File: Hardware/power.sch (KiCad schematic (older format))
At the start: 9 parts, among them J1 Barrel_Jack, U4 TL074, U5 LD1117S33CTR

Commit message: complete initial PCB layout. CapSense buttons still not done, but everything else should be there. I had to increase to a 4-layer board to keep the dimensions 8"x4".
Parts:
- removed D1: D, digikey-footprints:TO-252-3, symbol D
- added D1: D_Schottky, Diodes_SMD:D_SMB, symbol D_Schottky
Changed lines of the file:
@@
 Wire Wire Line
 	2150 1800 2100 1800
-$Comp
-L D D1
-U 1 1 5C392341
-P 2450 1600
-F 0 "D1" H 2450 1700 50  0000 C CNN
-F 1 "D" H 2450 1500 50  0000 C CNN
-F 2 "digikey-footprints:TO-252-3" H 2450 1600 50  0001 C CNN
-F 3 "" H 2450 1600 50  0001 C CNN
-	1    2450 1600
-	-1   0    0    1
-$EndComp
 Wire Wire Line
 	2700 1500 2700 1600
@@
 	1    0    0    1
 $EndComp
+$Comp
+L D_Schottky D1
+U 1 1 5C40562C
+P 2450 1600
+F 0 "D1" H 2450 1700 50  0000 C CNN
+F 1 "D_Schottky" H 2450 1500 50  0000 C CNN
+F 2 "Diodes_SMD:D_SMB" H 2450 1600 50  0001 C CNN
+F 3 "" H 2450 1600 50  0001 C CNN
+	1    2450 1600
+	-1   0    0    1
+$EndComp
 $EndSCHEMATC

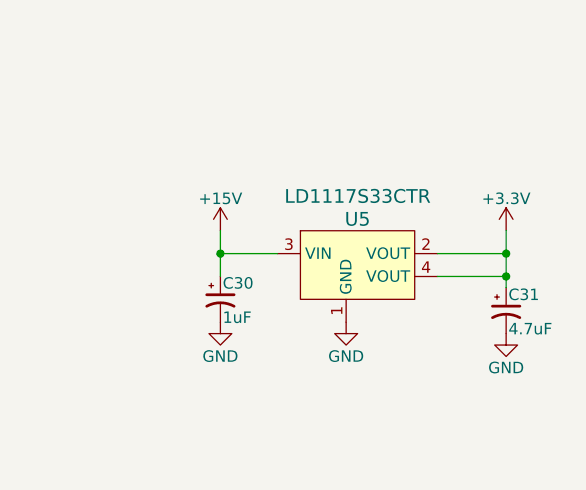
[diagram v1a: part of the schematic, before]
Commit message: change 3.3V to 5V, fix LFO biasing, LPF, JFET bias trim pots.
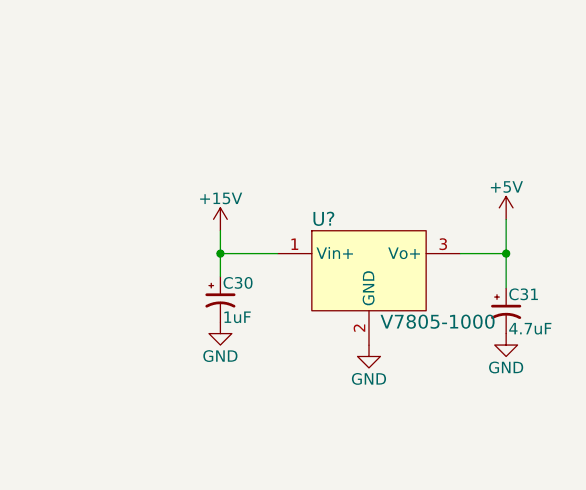
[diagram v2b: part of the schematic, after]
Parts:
- removed U5: LD1117S33CTR, digikey-footprints:SOT-223, symbol LD1117S33CTR
- added U?: V7805-1000, digikey-footprints:3-SIP_Module_V7805-1000, symbol V7805-1000
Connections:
- net +15V: now also U?.1 (Vin+)
- net GND: now also U?.2 (GND)
- net +3V3 renamed +5V
- net +5V: now also U?.3 (Vo+)
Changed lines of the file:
@@
 Connection ~ 1900 3150
-$Comp
-L LD1117S33CTR U5
-U 1 1 5C392D20
-P 5250 2750
-F 0 "U5" H 5300 2900 60  0000 C CNN
-F 1 "LD1117S33CTR" H 5300 3000 60  0000 C CNN
-F 2 "digikey-footprints:SOT-223" H 5450 2950 60  0001 L CNN
-F 3 "http://www.st.com/content/ccc/resource/technical/document/datasheet/99/3b/7d/91/91/51/4b/be/CD00000544.pdf/files/CD00000544.pdf/jcr:content/translations/en.CD00000544.pdf" H 5450 3050 60  0001 L CNN
-F 4 "497-1241-1-ND" H 5450 3150 60  0001 L CNN "Digi-Key_PN"
-F 5 "LD1117S33CTR" H 5450 3250 60  0001 L CNN "MPN"
-F 6 "Integrated Circuits (ICs)" H 5450 3350 60  0001 L CNN "Category"
-F 7 "PMIC - Voltage Regulators - Linear" H 5450 3450 60  0001 L CNN "Family"
-F 8 "http://www.st.com/content/ccc/resource/technical/document/datasheet/99/3b/7d/91/91/51/4b/be/CD00000544.pdf/files/CD00000544.pdf/jcr:content/translations/en.CD00000544.pdf" H 5450 3550 60  0001 L CNN "DK_Datasheet_Link"
-F 9 "/product-detail/en/stmicroelectronics/LD1117S33CTR/497-1241-1-ND/586241" H 5450 3650 60  0001 L CNN "DK_Detail_Page"
-F 10 "IC REG LINEAR 3.3V 800MA SOT223" H 5450 3750 60  0001 L CNN "Description"
-F 11 "STMicroelectronics" H 5450 3850 60  0001 L CNN "Manufacturer"
-F 12 "Active" H 5450 3950 60  0001 L CNN "Status"
-	1    5250 2750
-	1    0    0    -1
-$EndComp
 $Comp
 L CP1_Small C30
@@
 L GND #PWR044
 U 1 1 5C392F13
-P 5250 3050
-F 0 "#PWR044" H 5250 2800 50  0001 C CNN
-F 1 "GND" H 5250 2900 50  0000 C CNN
-F 2 "" H 5250 3050 50  0001 C CNN
-F 3 "" H 5250 3050 50  0001 C CNN
-	1    5250 3050
+P 5350 3150
+F 0 "#PWR044" H 5350 2900 50  0001 C CNN
+F 1 "GND" H 5350 3000 50  0000 C CNN
+F 2 "" H 5350 3150 50  0001 C CNN
+F 3 "" H 5350 3150 50  0001 C CNN
+	1    5350 3150
 	1    0    0    -1
 $EndComp
-$Comp
-L +3.3V #PWR045
-U 1 1 5C392F35
-P 5950 2650
-F 0 "#PWR045" H 5950 2500 50  0001 C CNN
-F 1 "+3.3V" H 5950 2790 50  0000 C CNN
-F 2 "" H 5950 2650 50  0001 C CNN
-F 3 "" H 5950 2650 50  0001 C CNN
-	1    5950 2650
-	1    0    0    -1
-$EndComp
-Wire Wire Line
-	5950 2650 5950 2900
-Wire Wire Line
-	5950 2750 5650 2750
-Wire Wire Line
-	5950 2850 5650 2850
-Connection ~ 5950 2750
 $Comp
 L CP1_Small C31
@@
 	1    0    0    -1
 $EndComp
-Connection ~ 5950 2850
 $Comp
 L GND #PWR046
@@
 	-1   0    0    1
 $EndComp
+$Comp
+L V7805-1000 U?
+U 1 1 5C548AF2
+P 5350 2850
+F 0 "U?" H 5100 3100 60  0000 L CNN
+F 1 "V7805-1000" H 5400 2650 60  0000 L CNN
+F 2 "digikey-footprints:3-SIP_Module_V7805-1000" H 5550 3050 60  0001 L CNN
+F 3 "https://www.cui.com/product/resource/digikeypdf/v78xx-1000.pdf" H 5550 3150 60  0001 L CNN
+F 4 "102-1715-ND" H 5550 3250 60  0001 L CNN "Digi-Key_PN"
+F 5 "V7805-1000" H 5550 3350 60  0001 L CNN "MPN"
+F 6 "Power Supplies - Board Mount" H 5550 3450 60  0001 L CNN "Category"
+F 7 "DC DC Converters" H 5550 3550 60  0001 L CNN "Family"
+F 8 "https://www.cui.com/product/resource/digikeypdf/v78xx-1000.pdf" H 5550 3650 60  0001 L CNN "DK_Datasheet_Link"
+F 9 "/product-detail/en/cui-inc/V7805-1000/102-1715-ND/1828608" H 5550 3750 60  0001 L CNN "DK_Detail_Page"
+F 10 "DC DC CONVERTER 5V 5W" H 5550 3850 60  0001 L CNN "Description"
+F 11 "CUI Inc." H 5550 3950 60  0001 L CNN "Manufacturer"
+F 12 "Active" H 5550 4050 60  0001 L CNN "Status"
+	1    5350 2850
+	1    0    0    -1
+$EndComp
+Wire Wire Line
+	5750 2750 5950 2750
+Wire Wire Line
+	5950 2600 5950 2900
+$Comp
+L +5V #PWR?
+U 1 1 5C548CA8
+P 5950 2600
+F 0 "#PWR?" H 5950 2450 50  0001 C CNN
+F 1 "+5V" H 5950 2740 50  0000 C CNN
+F 2 "" H 5950 2600 50  0001 C CNN
+F 3 "" H 5950 2600 50  0001 C CNN
+	1    5950 2600
+	1    0    0    -1
+$EndComp
+Connection ~ 5950 2750
 $EndSCHEMATC

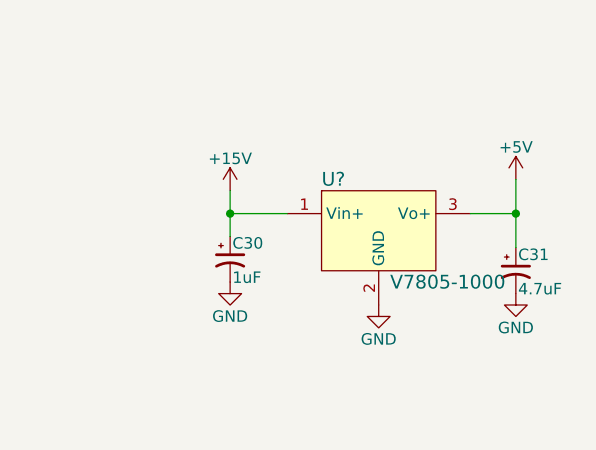
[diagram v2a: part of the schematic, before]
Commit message: add quantization switches
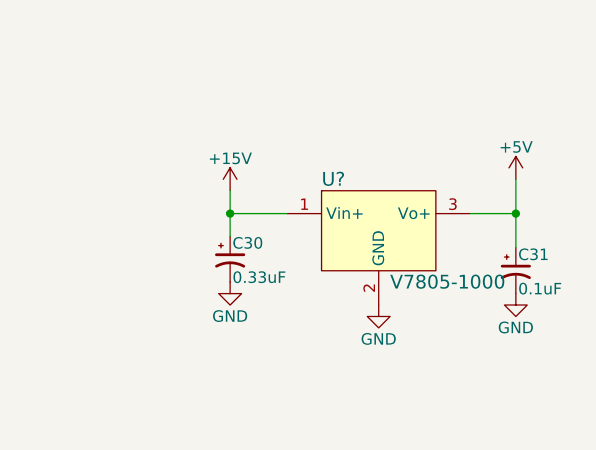
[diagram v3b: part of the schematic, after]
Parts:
- C30: value 1uF -> 0.33uF
- C31: value 4.7uF -> 0.1uF
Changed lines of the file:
@@
 P 4700 2950
 F 0 "C30" H 4710 3020 50  0000 L CNN
-F 1 "1uF" H 4710 2870 50  0000 L CNN
+F 1 "0.33uF" H 4710 2870 50  0000 L CNN
 F 2 "Capacitors_SMD:CP_Elec_4x4.5" H 4700 2950 50  0001 C CNN
 F 3 "" H 4700 2950 50  0001 C CNN
@@
 P 5950 3000
 F 0 "C31" H 5960 3070 50  0000 L CNN
-F 1 "4.7uF" H 5960 2920 50  0000 L CNN
+F 1 "0.1uF" H 5960 2920 50  0000 L CNN
 F 2 "Capacitors_SMD:CP_Elec_4x5.7" H 5950 3000 50  0001 C CNN
 F 3 "" H 5950 3000 50  0001 C CNN

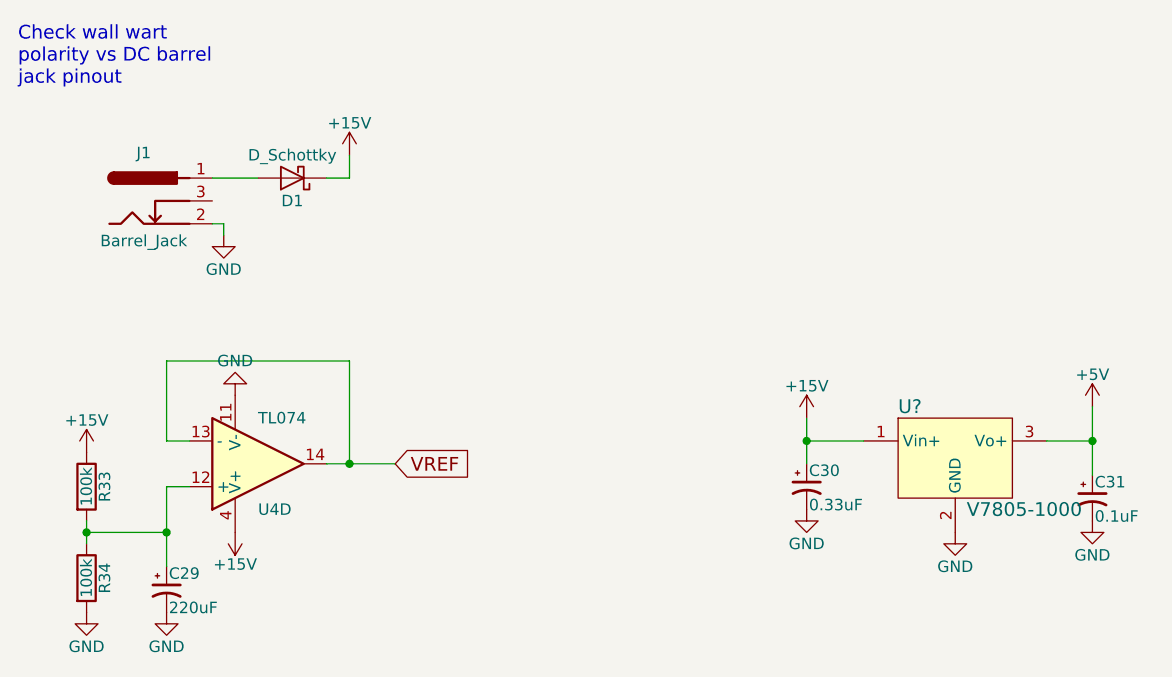
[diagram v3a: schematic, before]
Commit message: begin PCB v2 layout. fix ref designators, associate footprints on new components, create new PCB file, import components.
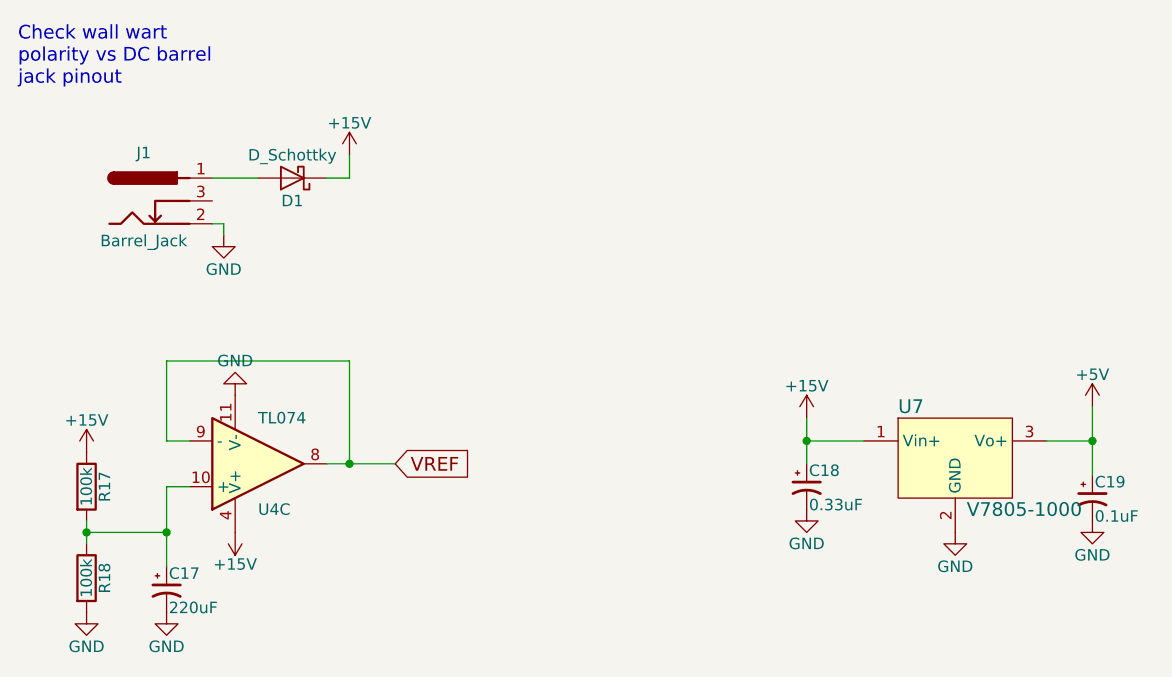
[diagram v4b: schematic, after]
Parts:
- gave numbers to parts that had none: 1
- renumbered C29 to C17, C30 to C18, C31 to C19, R33 to R17, R34 to R18
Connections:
- net VREF: now also U4.8, U4.9 (-); no longer U4.13 (-), U4.14
- net at C17.1, R17.2, R18.1: now also U4.10 (+); no longer U4.12 (+)
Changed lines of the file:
@@
 $EndComp
 $Comp
-L +15V #PWR037
+L +15V #PWR23
 U 1 1 5C3922F5
 P 2700 1500
-F 0 "#PWR037" H 2700 1350 50  0001 C CNN
+F 0 "#PWR23" H 2700 1350 50  0001 C CNN
 F 1 "+15V" H 2700 1640 50  0000 C CNN
 F 2 "" H 2700 1500 50  0001 C CNN
@@
 Check wall wart \npolarity vs DC barrel \njack pinout
 $Comp
-L GND #PWR038
+L GND #PWR20
 U 1 1 5C39231B
 P 2150 1850
-F 0 "#PWR038" H 2150 1600 50  0001 C CNN
+F 0 "#PWR20" H 2150 1600 50  0001 C CNN
 F 1 "GND" H 2150 1700 50  0000 C CNN
 F 2 "" H 2150 1850 50  0001 C CNN
@@
 	2700 1600 2600 1600
 $Comp
-L R R33
+L R R17
 U 1 1 5C3923A0
 P 1550 2950
-F 0 "R33" V 1630 2950 50  0000 C CNN
+F 0 "R17" V 1630 2950 50  0000 C CNN
 F 1 "100k" V 1550 2950 50  0000 C CNN
 F 2 "digikey-footprints:0805" V 1480 2950 50  0001 C CNN
@@
 $EndComp
 $Comp
-L R R34
+L R R18
 U 1 1 5C392430
 P 1550 3350
-F 0 "R34" V 1630 3350 50  0000 C CNN
+F 0 "R18" V 1630 3350 50  0000 C CNN
 F 1 "100k" V 1550 3350 50  0000 C CNN
 F 2 "digikey-footprints:0805" V 1480 3350 50  0001 C CNN
@@
 $EndComp
 $Comp
-L CP1_Small C29
+L CP1_Small C17
 U 1 1 5C392458
 P 1900 3400
-F 0 "C29" H 1910 3470 50  0000 L CNN
+F 0 "C17" H 1910 3470 50  0000 L CNN
 F 1 "220uF" H 1910 3320 50  0000 L CNN
 F 2 "Capacitors_SMD:CP_Elec_8x10" H 1900 3400 50  0001 C CNN
@@
 $EndComp
 $Comp
-L GND #PWR039
+L GND #PWR18
 U 1 1 5C392477
 P 1550 3500
-F 0 "#PWR039" H 1550 3250 50  0001 C CNN
+F 0 "#PWR18" H 1550 3250 50  0001 C CNN
 F 1 "GND" H 1550 3350 50  0000 C CNN
 F 2 "" H 1550 3500 50  0001 C CNN
@@
 $EndComp
 $Comp
-L GND #PWR040
+L GND #PWR19
 U 1 1 5C392498
 P 1900 3500
-F 0 "#PWR040" H 1900 3250 50  0001 C CNN
+F 0 "#PWR19" H 1900 3250 50  0001 C CNN
 F 1 "GND" H 1900 3350 50  0000 C CNN
 F 2 "" H 1900 3500 50  0001 C CNN
@@
 $EndComp
 $Comp
-L +15V #PWR041
+L +15V #PWR17
 U 1 1 5C3924B7
 P 1550 2800
-F 0 "#PWR041" H 1550 2650 50  0001 C CNN
+F 0 "#PWR17" H 1550 2650 50  0001 C CNN
 F 1 "+15V" H 1550 2940 50  0000 C CNN
 F 2 "" H 1550 2800 50  0001 C CNN
@@
 Connection ~ 1900 3150
 $Comp
-L CP1_Small C30
+L CP1_Small C18
 U 1 1 5C392DFE
 P 4700 2950
-F 0 "C30" H 4710 3020 50  0000 L CNN
+F 0 "C18" H 4710 3020 50  0000 L CNN
 F 1 "0.33uF" H 4710 2870 50  0000 L CNN
 F 2 "Capacitors_SMD:CP_Elec_4x4.5" H 4700 2950 50  0001 C CNN
@@
 	4700 2750 4950 2750
 $Comp
-L +15V #PWR042
+L +15V #PWR24
 U 1 1 5C392EAE
 P 4700 2650
-F 0 "#PWR042" H 4700 2500 50  0001 C CNN
+F 0 "#PWR24" H 4700 2500 50  0001 C CNN
 F 1 "+15V" H 4700 2790 50  0000 C CNN
 F 2 "" H 4700 2650 50  0001 C CNN
@@
 Connection ~ 4700 2750
 $Comp
-L GND #PWR043
+L GND #PWR25
 U 1 1 5C392EE5
 P 4700 3050
-F 0 "#PWR043" H 4700 2800 50  0001 C CNN
+F 0 "#PWR25" H 4700 2800 50  0001 C CNN
 F 1 "GND" H 4700 2900 50  0000 C CNN
 F 2 "" H 4700 3050 50  0001 C CNN
@@
 $EndComp
 $Comp
-L GND #PWR044
+L GND #PWR26
 U 1 1 5C392F13
 P 5350 3150
-F 0 "#PWR044" H 5350 2900 50  0001 C CNN
+F 0 "#PWR26" H 5350 2900 50  0001 C CNN
 F 1 "GND" H 5350 3000 50  0000 C CNN
 F 2 "" H 5350 3150 50  0001 C CNN
@@
 $EndComp
 $Comp
-L CP1_Small C31
+L CP1_Small C19
 U 1 1 5C392F95
 P 5950 3000
-F 0 "C31" H 5960 3070 50  0000 L CNN
+F 0 "C19" H 5960 3070 50  0000 L CNN
 F 1 "0.1uF" H 5960 2920 50  0000 L CNN
 F 2 "Capacitors_SMD:CP_Elec_4x5.7" H 5950 3000 50  0001 C CNN
@@
 $EndComp
 $Comp
-L GND #PWR046
+L GND #PWR28
 U 1 1 5C393000
 P 5950 3100
-F 0 "#PWR046" H 5950 2850 50  0001 C CNN
+F 0 "#PWR28" H 5950 2850 50  0001 C CNN
 F 1 "GND" H 5950 2950 50  0000 C CNN
 F 2 "" H 5950 3100 50  0001 C CNN
@@
 $EndComp
 $Comp
-L GND #PWR047
+L GND #PWR21
 U 1 1 5C39BA81
 P 2200 2550
-F 0 "#PWR047" H 2200 2300 50  0001 C CNN
+F 0 "#PWR21" H 2200 2300 50  0001 C CNN
 F 1 "GND" H 2200 2400 50  0000 C CNN
 F 2 "" H 2200 2550 50  0001 C CNN
@@
 $EndComp
 $Comp
-L +15V #PWR048
+L +15V #PWR22
 U 1 1 5C39BAA7
 P 2200 3150
-F 0 "#PWR048" H 2200 3000 50  0001 C CNN
+F 0 "#PWR22" H 2200 3000 50  0001 C CNN
 F 1 "+15V" H 2200 3290 50  0000 C CNN
 F 2 "" H 2200 3150 50  0001 C CNN
@@
 $Comp
 L TL074 U4
-U 4 1 5C3D82DF
+U 3 1 5C3D82DF
 P 2300 2850
 F 0 "U4" H 2300 3050 50  0000 L CNN
@@
 F 2 "digikey-footprints:SOIC-14_W3.9mm" H 2250 2950 50  0001 C CNN
 F 3 "" H 2350 3050 50  0001 C CNN
-	4    2300 2850
+	3    2300 2850
 	1    0    0    1
 $EndComp
@@
 $EndComp
 $Comp
-L V7805-1000 U?
+L V7805-1000 U7
 U 1 1 5C548AF2
 P 5350 2850
-F 0 "U?" H 5100 3100 60  0000 L CNN
+F 0 "U7" H 5100 3100 60  0000 L CNN
 F 1 "V7805-1000" H 5400 2650 60  0000 L CNN
 F 2 "digikey-footprints:3-SIP_Module_V7805-1000" H 5550 3050 60  0001 L CNN
@@
 	5950 2600 5950 2900
 $Comp
-L +5V #PWR?
+L +5V #PWR27
 U 1 1 5C548CA8
 P 5950 2600
-F 0 "#PWR?" H 5950 2450 50  0001 C CNN
+F 0 "#PWR27" H 5950 2450 50  0001 C CNN
 F 1 "+5V" H 5950 2740 50  0000 C CNN
 F 2 "" H 5950 2600 50  0001 C CNN
